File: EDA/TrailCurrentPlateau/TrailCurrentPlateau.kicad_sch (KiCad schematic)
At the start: 12 parts, among them J1 DHT22, U1 Amazon Buck Converter, U2 ESP32-C6-Super-Mini, U3 SN65HVD230, U4 ZX-XH2.54-4PWT

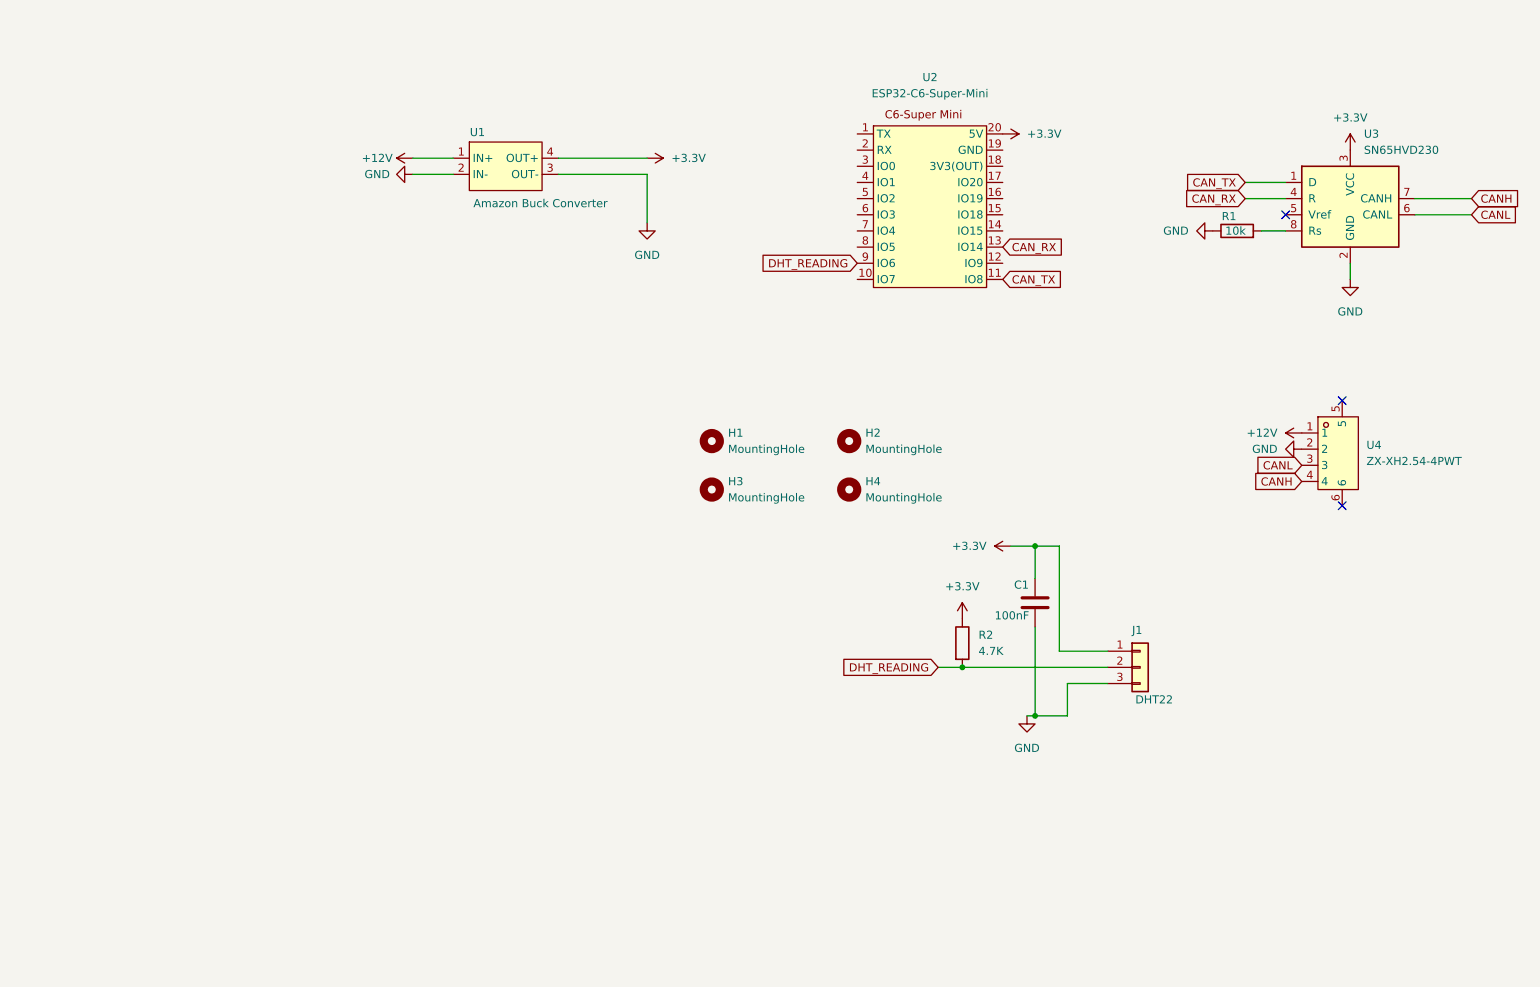
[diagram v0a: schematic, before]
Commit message: Moved to ESP32S3 Zero board, adafruit bno055 and standard approach for CAN Bus and OTA
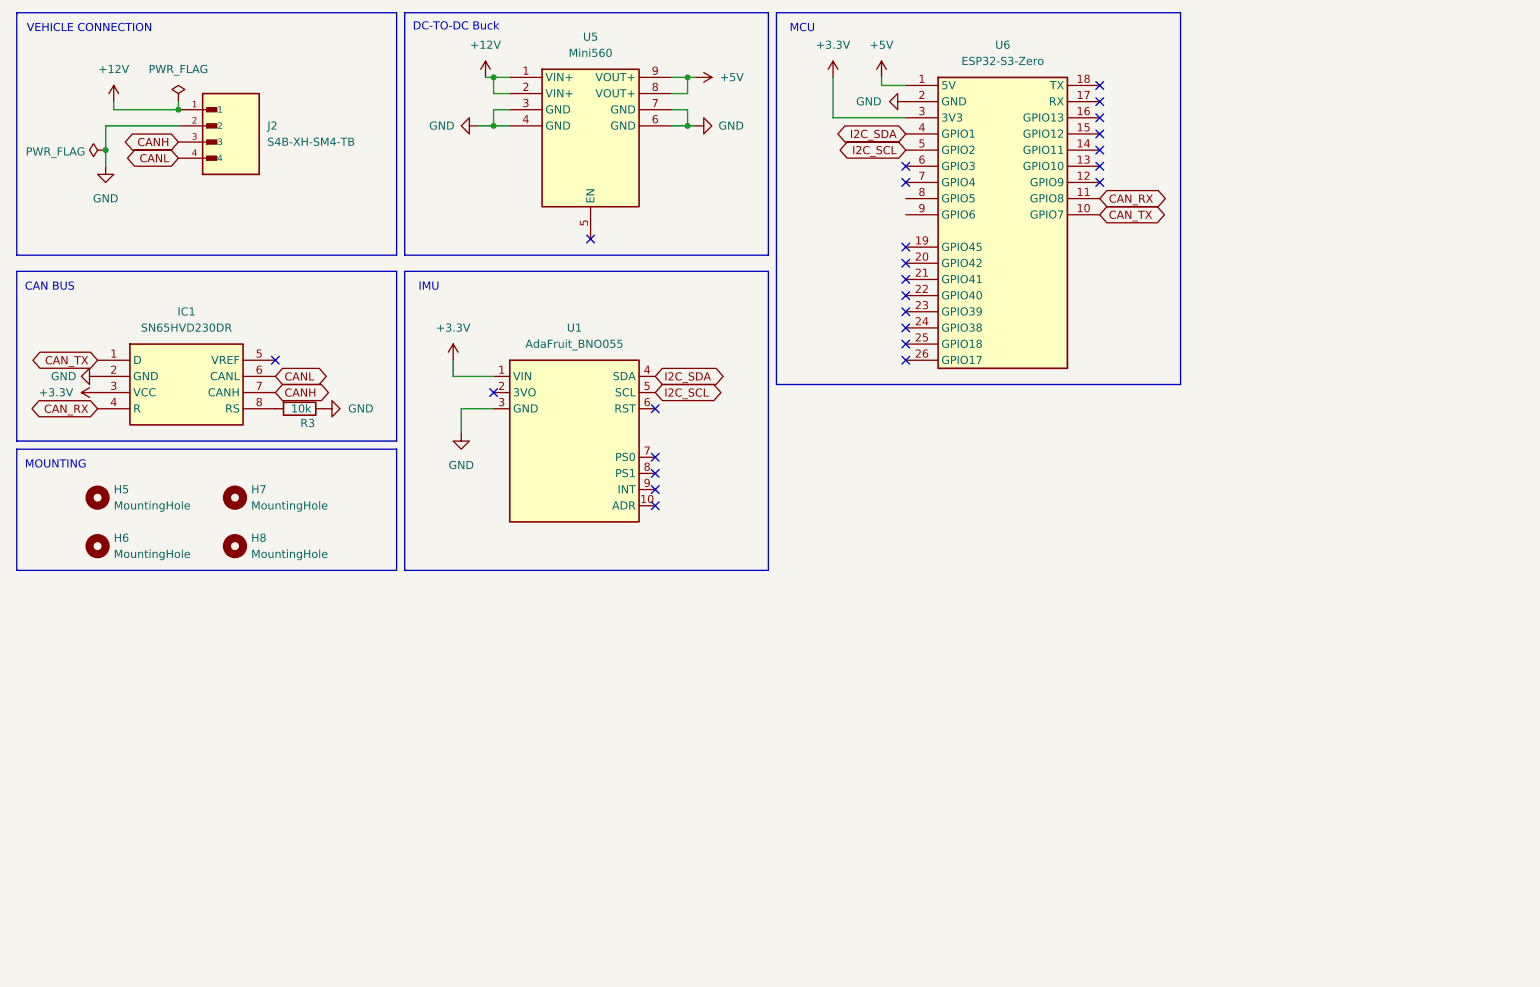
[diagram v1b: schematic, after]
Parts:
- removed C1: 100nF, Capacitor_SMD:C_1206_3216Metric_Pad1.33x1.80mm_HandSolder, symbol Device:C
- removed H1, H2, H3, H4: MountingHole, MountingHole:MountingHole_2.5mm, symbol Mechanical:MountingHole
- removed J1: DHT22, Connector_PinHeader_2.54mm:PinHeader_1x03_P2.54mm_Vertical, symbol Connector_Generic:Conn_01x03
- removed R1: 10k, Resistor_SMD:R_1206_3216Metric_Pad1.30x1.75mm_HandSolder, symbol Device:R
- removed R2: 4.7K, Capacitor_SMD:C_1206_3216Metric_Pad1.33x1.80mm_HandSolder, symbol Device:R
- removed U1: Amazon Buck Converter, Converter_DCDC:AmazonBuckConverter, symbol Regulator_Switching:AmazonBuckConverter
- removed U2: ESP32-C6-Super-Mini, RF_Module:ESP32-C6-Super-Mini, symbol RF_Module:ESP32-C6-Super-Mini
- removed U3: SN65HVD230, Package_SO:SOIC-8_3.9x4.9mm_P1.27mm, symbol Interface_CAN_LIN:SN65HVD230
- removed U4: ZX-XH2.54-4PWT, easyeda2kicad:CONN-SMD_4P-P2.50-WAFER-254W-4P, symbol LCSC:ZX-XH2.54-4PWT
- added H5, H6, H7, H8: MountingHole, MountingHole:MountingHole_2.5mm, symbol Mechanical:MountingHole
- added IC1: SN65HVD230DR, TrailCurrentFootprints:SN65HVD230DR, symbol TrailCurrentSymbolLibrary:SN65HVD230DR
- added J2: S4B-XH-SM4-TB, TrailCurrentFootprints:JST_S4B-XH-SM4-TB, symbol TrailCurrentSymbolLibrary:S4B-XH-SM4-TB
- added R3: 10k, Resistor_SMD:R_1206_3216Metric_Pad1.30x1.75mm_HandSolder, symbol Device:R
- added U1: AdaFruit_BNO055, TrailCurrentFootprints:AdaFruit_BNO055, symbol TrailCurrentSymbolLibrary:AdaFruit_BNO055
- added U5: Mini560, TrailCurrentFootprints:Mini560, symbol TrailCurrentSymbolLibrary:Mini560
- added U6: ESP32-S3-Zero, TrailCurrentFootprints:ESP32-S3-Zero_SMD, symbol TrailCurrentSymbolLibrary:ESP32-S3-Zero
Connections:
- net +12V: now also J2.1, U5.1 (VIN+), U5.2 (VIN+)
- net +3.3V: now also IC1.3 (VCC), U1.1 (VIN), U6.3 (3V3)
- net CANH: now also IC1.7 (CANH), J2.3
- net CANL: now also IC1.6 (CANL), J2.4
- net CAN_RX: now also IC1.4 (R), U6.11 (GPIO8)
- net CAN_TX: now also IC1.1 (D), U6.10 (GPIO7)
- net GND: now also IC1.2 (GND), J2.2, R3.1, U1.3 (GND), U5.3 (GND), U5.4 (GND), U5.6 (GND), U5.7 (GND), U6.2 (GND)
- new net: IC1.8 (RS), R3.2
- new net +5V: U5.8 (VOUT+), U5.9 (VOUT+), U6.1 (5V)
- new net I2C_SCL: U1.5 (SCL), U6.5 (GPIO2)
- new net I2C_SDA: U1.4 (SDA), U6.4 (GPIO1)
- no-connect marks 3 -> 25
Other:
- note added: "CAN BUS"
- note added: "DC-TO-DC Buck"
- note added: "IMU"
- note added: "MCU"
- note added: "MOUNTING"
- note added: "VEHICLE CONNECTION"

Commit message: Updates to improve the calibration process and communicate that to headwaters.
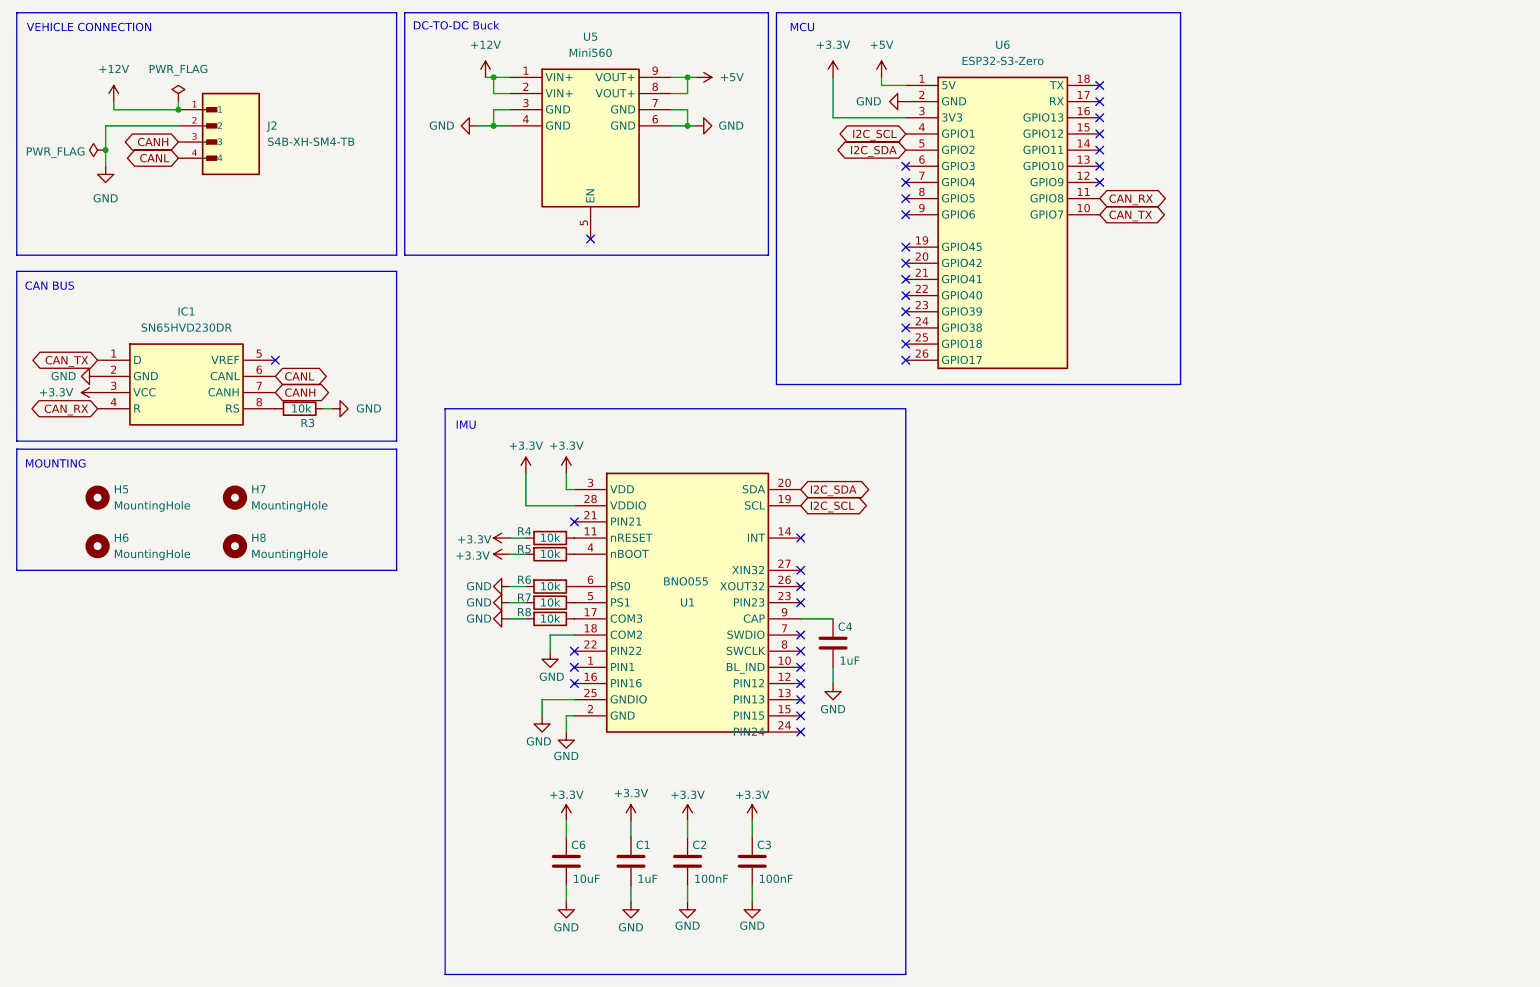
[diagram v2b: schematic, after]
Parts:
- removed U1: AdaFruit_BNO055, TrailCurrentFootprints:AdaFruit_BNO055, symbol TrailCurrentSymbolLibrary:AdaFruit_BNO055
- added C1, C4: 1uF, Capacitor_SMD:C_1206_3216Metric, symbol Device:C
- added C2, C3: 100nF, Capacitor_SMD:C_1206_3216Metric, symbol Device:C
- added C6: 10uF, Capacitor_SMD:C_1206_3216Metric, symbol Device:C
- added R4, R5, R6, R7, R8: 10k, Resistor_SMD:R_1206_3216Metric_Pad1.30x1.75mm_HandSolder, symbol Device:R
- added U1: BNO055, TrailCurrentFootprints:BNO055_LGA-28_3.8x5.2mm, symbol TrailCurrentSymbolLibrary:BNO055
- U6: footprint TrailCurrentFootprints:ESP32-S3-Zero_SMD -> TrailCurrentFootprints:ESP32-S3-Zero_TH
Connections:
- net +3.3V: now also C1.1, C2.1, C3.1, C6.1, R4.2, R5.2, U1.28 (VDDIO), U1.3 (VDD)
- net GND: now also C1.2, C2.2, C3.2, C4.2, C6.2, R6.2, R7.2, R8.2, U1.18 (COM2), U1.2 (GND), U1.25 (GNDIO)
- net I2C_SCL: now also U6.4 (GPIO1), U1.19 (SCL); no longer U6.5 (GPIO2)
- net I2C_SDA: now also U6.5 (GPIO2), U1.20 (SDA); no longer U6.4 (GPIO1)
- new net: C4.1, U1.9 (CAP)
- new net: R5.1, U1.4 (nBOOT)
- new net: R8.1, U1.17 (COM3)
- new net: R7.1, U1.5 (PS1)
- new net: R4.1, U1.11 (nRESET)
- new net: R6.1, U1.6 (PS0)
- no-connect marks 25 -> 36
